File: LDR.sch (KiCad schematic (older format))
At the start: 2 parts

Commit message: añaadido zocalo para sensor de temperatura y primera distribucion sobre la PCB
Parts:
- R20: footprint Resistencias:Resistencia_1_4_W_10_mm -> Resistors_SMD:R_0805
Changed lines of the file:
@@
 $Descr User 8268 5846
 encoding utf-8
-Sheet 7 13
+Sheet 7 14
 Title ""
 Date ""
@@
 F 0 "R20" V 3330 2900 50  0000 C CNN
 F 1 "1K" V 3250 2900 50  0000 C CNN
-F 2 "Resistencias:Resistencia_1_4_W_10_mm" V 3180 2900 50  0001 C CNN
+F 2 "Resistors_SMD:R_0805" V 3180 2900 50  0001 C CNN
 F 3 "" H 3250 2900 50  0000 C CNN
 F 4 "SR_PASSIVES" H 3250 2900 60  0001 C CNN "Fabricante"

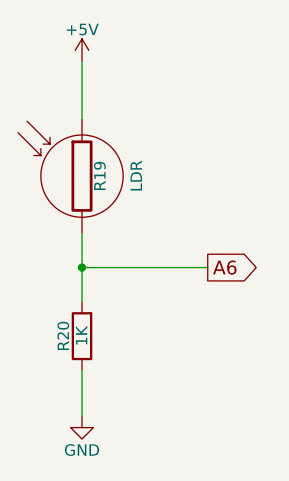
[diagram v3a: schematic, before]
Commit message: ordenar referencias de componentes
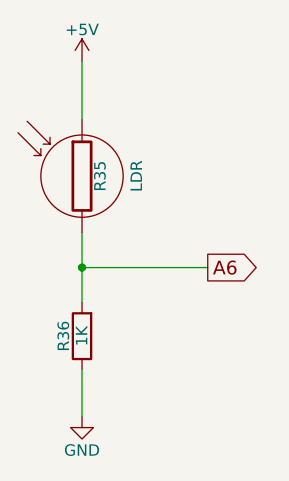
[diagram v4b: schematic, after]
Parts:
- R35: renamed from R19; Fabricante TOKEN -> WODEYIJIA; Ref PGM5516 -> GM7516; Ref_Proveedor PGM5516 -> GM7516
- R36: renamed from R20; Fabricante SR_PASSIVES -> VISHAY; Potencia 1/4W -> 1/8W; Ref_Proveedor CF1/4W-1K -> CRCW08051K00FKEA; Tolerancia 5% -> 1%
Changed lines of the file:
@@
 $Descr User 8268 5846
 encoding utf-8
-Sheet 7 15
+Sheet 14 15
 Title ""
 Date ""
@@
 $EndDescr
 $Comp
-L Photores R19
+L Photores R35
 U 1 1 5793F436
 P 3250 2200
-F 0 "R19" V 3330 2200 50  0000 C CNN
+F 0 "R35" V 3330 2200 50  0000 C CNN
 F 1 "LDR" V 3460 2200 50  0000 C TNN
 F 2 "Sensores:LDR_TOKEN_PGM5_Series" V 3180 2200 50  0001 C CNN
 F 3 "" H 3250 2200 50  0000 C CNN
-F 4 "TOKEN" H 3250 2200 60  0001 C CNN "Fabricante"
-F 5 "PGM5516" H 3250 2200 60  0001 C CNN "Ref"
+F 4 "WODEYIJIA" H 3250 2200 60  0001 C CNN "Fabricante"
+F 5 "GM7516" H 3250 2200 60  0001 C CNN "Ref"
 F 6 "~" H 3250 2200 60  0001 C CNN "Potencia"
 F 7 "~" H 3250 2200 60  0001 C CNN "Tolerancia"
 F 8 "TME" H 3250 2200 60  0001 C CNN "Provedor"
-F 9 "PGM5516" H 3250 2200 60  0001 C CNN "Ref_Proveedor"
+F 9 "GM7516" H 3250 2200 60  0001 C CNN "Ref_Proveedor"
 	1    3250 2200
 	1    0    0    -1
 $EndComp
 $Comp
-L GND #PWR013
+L GND #PWR56
 U 1 1 5793F43D
 P 3250 3250
-F 0 "#PWR013" H 3250 3000 50  0001 C CNN
+F 0 "#PWR56" H 3250 3000 50  0001 C CNN
 F 1 "GND" H 3250 3100 50  0000 C CNN
 F 2 "" H 3250 3250 50  0000 C CNN
@@
 $EndComp
 $Comp
-L +5V #PWR014
+L +5V #PWR55
 U 1 1 5793F443
 P 3250 1700
-F 0 "#PWR014" H 3250 1550 50  0001 C CNN
+F 0 "#PWR55" H 3250 1550 50  0001 C CNN
 F 1 "+5V" H 3250 1840 50  0000 C CNN
 F 2 "" H 3250 1700 50  0000 C CNN
@@
 	3250 2450 3250 2750
 $Comp
-L R R20
+L R R36
 U 1 1 5793F455
 P 3250 2900
-F 0 "R20" V 3330 2900 50  0000 C CNN
+F 0 "R36" V 3330 2900 50  0000 C CNN
 F 1 "1K" V 3250 2900 50  0000 C CNN
 F 2 "Resistors_SMD:R_0805" V 3180 2900 50  0001 C CNN
 F 3 "" H 3250 2900 50  0000 C CNN
-F 4 "SR_PASSIVES" H 3250 2900 60  0001 C CNN "Fabricante"
+F 4 "VISHAY" H 3250 2900 60  0001 C CNN "Fabricante"
 F 5 "CF1/4W-1K" H 3250 2900 60  0001 C CNN "Ref"
-F 6 "1/4W" H 3250 2900 60  0001 C CNN "Potencia"
-F 7 "5%" H 3250 2900 60  0001 C CNN "Tolerancia"
+F 6 "1/8W" H 3250 2900 60  0001 C CNN "Potencia"
+F 7 "1%" H 3250 2900 60  0001 C CNN "Tolerancia"
 F 8 "TME" H 3250 2900 60  0001 C CNN "Provedor"
-F 9 "CF1/4W-1K" H 3250 2900 60  0001 C CNN "Ref_Proveedor"
+F 9 "CRCW08051K00FKEA" H 3250 2900 60  0001 C CNN "Ref_Proveedor"
 	1    3250 2900
 	-1   0    0    1

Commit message: cambiados encoder y potenciometro
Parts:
- R36: footprint Resistors_SMD:R_0805 -> Resistencias:R_0805
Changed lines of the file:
@@
 $EndComp
 $Comp
-L GND #PWR56
+L GND #PWR057
 U 1 1 5793F43D
 P 3250 3250
-F 0 "#PWR56" H 3250 3000 50  0001 C CNN
+F 0 "#PWR057" H 3250 3000 50  0001 C CNN
 F 1 "GND" H 3250 3100 50  0000 C CNN
 F 2 "" H 3250 3250 50  0000 C CNN
@@
 $EndComp
 $Comp
-L +5V #PWR55
+L +5V #PWR058
 U 1 1 5793F443
 P 3250 1700
-F 0 "#PWR55" H 3250 1550 50  0001 C CNN
+F 0 "#PWR058" H 3250 1550 50  0001 C CNN
 F 1 "+5V" H 3250 1840 50  0000 C CNN
 F 2 "" H 3250 1700 50  0000 C CNN
@@
 F 0 "R36" V 3330 2900 50  0000 C CNN
 F 1 "1K" V 3250 2900 50  0000 C CNN
-F 2 "Resistors_SMD:R_0805" V 3180 2900 50  0001 C CNN
+F 2 "Resistencias:R_0805" V 3180 2900 50  0001 C CNN
 F 3 "" H 3250 2900 50  0000 C CNN
 F 4 "VISHAY" H 3250 2900 60  0001 C CNN "Fabricante"

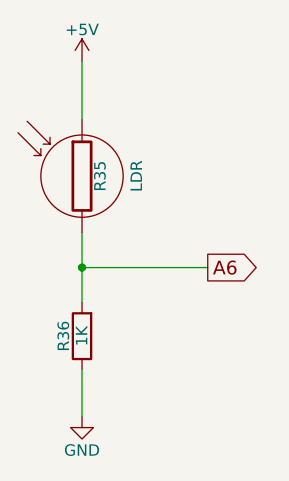
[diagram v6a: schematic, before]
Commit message: añadidos driver para led y conectores para fotodiodos infrarrojos
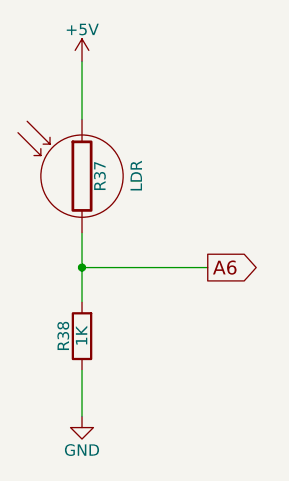
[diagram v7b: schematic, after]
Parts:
- renumbered R35 to R37, R36 to R38
